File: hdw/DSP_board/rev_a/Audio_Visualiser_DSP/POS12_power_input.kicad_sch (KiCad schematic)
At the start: 21 parts, among them J201 +12V IN, U201 TPS26600RHFT

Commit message: cleared stale digikey part numbers
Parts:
- C201: Dielectric X5R -> X7R; Digi-Key PN 445-12201-1-ND -> (none)
- C202: Dielectric X5R -> X7R; Digi-Key PN 490-10697-1-ND -> (none)
- C203: Digi-Key PN 718-1102-1-ND -> (none)
- R201: Digi-Key PN RMCF0402FT51K1CT-ND -> (none)
- R202: Digi-Key PN RMCF0402FT1K15CT-ND -> (none)
- R203: Digi-Key PN RMCF0402FT5K11CT-ND -> (none)
- R204, R206, R211: Digi-Key PN RMCF0402FT10K0CT-ND -> (none)
- R205, R210: Digi-Key PN RMCF0402FT10R0CT-ND -> (none)
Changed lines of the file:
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@@
 			)
 		)
-		(property "Digi-Key PN" "RMCF0402FT5K11CT-ND"
+		(property "Digi-Key PN" ""
 			(at 85.09 100.33 0)
 			(hide yes)
@@
 			)
 		)
-		(property "Digi-Key PN" "RMCF0402FT10R0CT-ND"
+		(property "Digi-Key PN" ""
 			(at 157.48 48.26 0)
 			(hide yes)
@@
 			)
 		)
-		(property "Digi-Key PN" "490-10697-1-ND"
+		(property "Digi-Key PN" ""
 			(at 127.635 139.7 0)
 			(hide yes)
@@
 			)
 		)
-		(property "Dielectric" "X5R"
+		(property "Dielectric" "X7R"
 			(at 142.24 154.94 0)
 			(show_name no)
@@
 			)
 		)
-		(property "Digi-Key PN" "RMCF0402FT51K1CT-ND"
+		(property "Digi-Key PN" ""
 			(at 85.09 57.15 0)
 			(hide yes)
@@
 			)
 		)
-		(property "Digi-Key PN" "RMCF0402FT10K0CT-ND"
+		(property "Digi-Key PN" ""
 			(at 190.5 121.92 0)
 			(hide yes)
@@
 			)
 		)
-		(property "Digi-Key PN" "718-1102-1-ND"
+		(property "Digi-Key PN" ""
 			(at 212.09 62.23 0)
 			(hide yes)
@@
 			)
 		)
-		(property "Digi-Key PN" "RMCF0402FT10R0CT-ND"
+		(property "Digi-Key PN" ""
 			(at 170.18 48.26 0)
 			(hide yes)
@@
 			)
 		)
-		(property "Digi-Key PN" "RMCF0402FT10K0CT-ND"
+		(property "Digi-Key PN" ""
 			(at 170.18 121.92 0)
 			(hide yes)
@@
 			)
 		)
-		(property "Digi-Key PN" "RMCF0402FT1K15CT-ND"
+		(property "Digi-Key PN" ""
 			(at 85.09 78.74 0)
 			(hide yes)
@@
 			)
 		)
-		(property "Dielectric" "X5R"
+		(property "Dielectric" "X7R"
 			(at 109.22 113.03 0)
 			(show_name no)
@@
 			)
 		)
-		(property "Digi-Key PN" "445-12201-1-ND"
+		(property "Digi-Key PN" ""
 			(at 123.825 97.79 0)
 			(hide yes)
@@
 			)
 		)
-		(property "Digi-Key PN" "RMCF0402FT10K0CT-ND"
+		(property "Digi-Key PN" ""
 			(at 105.41 57.15 0)
 			(hide yes)

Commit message: assigned many digi-key part numbers
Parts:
- C201: Digi-Key PN (none) -> 490-4516-1-ND
- C202: Digi-Key PN (none) -> 1276-CL05B104KB5NNNCCT-ND
- C203: Digi-Key PN (none) -> 399-8410-1-ND; Voltage 16V -> 25V
- R201: Digi-Key PN (none) -> 311-51.1KLRCT-ND
- R202: Digi-Key PN (none) -> 311-1.15KLRCT-ND
- R203: Digi-Key PN (none) -> 311-5.11KLRCT-ND
- R204, R206, R208, R211: Digi-Key PN (none) -> 311-10.0KLRCT-ND
- R205, R210: Digi-Key PN (none) -> 311-10.0LRCT-ND
- R209: Digi-Key PN (none) -> 311-3.65KLRCT-ND
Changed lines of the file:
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@@
 			)
 		)
-		(property "Digi-Key PN" ""
+		(property "Digi-Key PN" "311-5.11KLRCT-ND"
 			(at 85.09 100.33 0)
 			(hide yes)
@@
 			)
 		)
-		(property "Digi-Key PN" ""
+		(property "Digi-Key PN" "311-10.0KLRCT-ND"
 			(at 163.83 99.06 0)
 			(hide yes)
@@
 			)
 		)
-		(property "Digi-Key PN" ""
+		(property "Digi-Key PN" "311-10.0LRCT-ND"
 			(at 157.48 48.26 0)
 			(hide yes)
@@
 			)
 		)
-		(property "Digi-Key PN" ""
+		(property "Digi-Key PN" "311-3.65KLRCT-ND"
 			(at 171.45 100.33 0)
 			(hide yes)
@@
 			)
 		)
-		(property "Digi-Key PN" ""
+		(property "Digi-Key PN" "1276-CL05B104KB5NNNCCT-ND"
 			(at 127.635 139.7 0)
 			(hide yes)
@@
 			)
 		)
-		(property "Digi-Key PN" ""
+		(property "Digi-Key PN" "311-51.1KLRCT-ND"
 			(at 85.09 57.15 0)
 			(hide yes)
@@
 			)
 		)
-		(property "Digi-Key PN" ""
+		(property "Digi-Key PN" "311-10.0KLRCT-ND"
 			(at 190.5 121.92 0)
 			(hide yes)
@@
 			)
 		)
-		(property "Digi-Key PN" ""
+		(property "Digi-Key PN" "399-8410-1-ND"
 			(at 212.09 62.23 0)
 			(hide yes)
@@
 			)
 		)
-		(property "Voltage" "16V"
+		(property "Voltage" "25V"
 			(at 208.28 62.23 0)
 			(show_name no)
@@
 			)
 		)
-		(property "Digi-Key PN" ""
+		(property "Digi-Key PN" "311-10.0LRCT-ND"
 			(at 170.18 48.26 0)
 			(hide yes)
@@
 			)
 		)
-		(property "Digi-Key PN" ""
+		(property "Digi-Key PN" "311-10.0KLRCT-ND"
 			(at 170.18 121.92 0)
 			(hide yes)
@@
 			)
 		)
-		(property "Digi-Key PN" ""
+		(property "Digi-Key PN" "311-1.15KLRCT-ND"
 			(at 85.09 78.74 0)
 			(hide yes)
@@
 			)
 		)
-		(property "Digi-Key PN" ""
+		(property "Digi-Key PN" "490-4516-1-ND"
 			(at 123.825 97.79 0)
 			(hide yes)
@@
 			)
 		)
-		(property "Digi-Key PN" ""
+		(property "Digi-Key PN" "311-10.0KLRCT-ND"
 			(at 105.41 57.15 0)
 			(hide yes)

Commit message: Defined legit KiCad BOM variants
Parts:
- R205, R210: now not fitted
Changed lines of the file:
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@@
 					(reference "R203")
 					(unit 1)
+					(variant
+						(name "Default")
+					)
+					(variant
+						(name "Development")
+					)
 				)
 			)
@@
 					(reference "U201")
 					(unit 1)
+					(variant
+						(name "Default")
+					)
+					(variant
+						(name "Development")
+					)
 				)
 			)
@@
 					(reference "R208")
 					(unit 1)
+					(variant
+						(name "Default")
+					)
+					(variant
+						(name "Development")
+					)
 				)
 			)
@@
 					(reference "N201")
 					(unit 1)
+					(variant
+						(name "Default")
+					)
+					(variant
+						(name "Development")
+					)
 				)
 			)
@@
 		(on_board yes)
 		(in_pos_files yes)
-		(dnp no)
+		(dnp yes)
 		(property "Reference" "R205"
 			(at 160.02 48.26 90)
@@
 					(reference "R205")
 					(unit 1)
+					(variant
+						(name "Default")
+					)
+					(variant
+						(name "Development")
+						(dnp no)
+					)
 				)
 			)
@@
 					(reference "R209")
 					(unit 1)
+					(variant
+						(name "Default")
+					)
+					(variant
+						(name "Development")
+					)
 				)
 			)
@@
 					(reference "J201")
 					(unit 1)
+					(variant
+						(name "Default")
+					)
+					(variant
+						(name "Development")
+					)
 				)
 			)
@@
 					(reference "C202")
 					(unit 1)
+					(variant
+						(name "Default")
+					)
+					(variant
+						(name "Development")
+					)
 				)
 			)
@@
 					(reference "R207")
 					(unit 1)
+					(variant
+						(name "Default")
+					)
+					(variant
+						(name "Development")
+					)
 				)
 			)
@@
 					(reference "R201")
 					(unit 1)
+					(variant
+						(name "Default")
+					)
+					(variant
+						(name "Development")
+					)
 				)
 			)
@@
 					(reference "TP201")
 					(unit 1)
+					(variant
+						(name "Default")
+					)
+					(variant
+						(name "Development")
+					)
 				)
 			)
@@
 					(reference "D201")
 					(unit 1)
+					(variant
+						(name "Default")
+					)
+					(variant
+						(name "Development")
+					)
 				)
 			)
@@
 					(reference "TP202")
 					(unit 1)
+					(variant
+						(name "Default")
+					)
+					(variant
+						(name "Development")
+					)
 				)
 			)
@@
 					(reference "R211")
 					(unit 1)
+					(variant
+						(name "Default")
+					)
+					(variant
+						(name "Development")
+					)
 				)
 			)
@@
 					(reference "TP203")
 					(unit 1)
+					(variant
+						(name "Default")
+					)
+					(variant
+						(name "Development")
+					)
 				)
 			)
@@
 					(reference "C203")
 					(unit 1)
+					(variant
+						(name "Default")
+					)
+					(variant
+						(name "Development")
+					)
 				)
 			)
@@
 		(on_board yes)
 		(in_pos_files yes)
-		(dnp no)
+		(dnp yes)
 		(property "Reference" "R210"
 			(at 172.72 48.26 90)
@@
 					(reference "R210")
 					(unit 1)
+					(variant
+						(name "Default")
+					)
+					(variant
+						(name "Development")
+						(dnp no)
+					)
 				)
 			)
@@
 					(reference "R206")
 					(unit 1)
+					(variant
+						(name "Default")
+					)
+					(variant
+						(name "Development")
+					)
 				)
 			)
@@
 					(reference "R202")
 					(unit 1)
+					(variant
+						(name "Default")
+					)
+					(variant
+						(name "Development")
+					)
 				)
 			)
@@
 					(reference "C201")
 					(unit 1)
+					(variant
+						(name "Default")
+					)
+					(variant
+						(name "Development")
+					)
 				)
 			)
@@
 					(reference "R204")
 					(unit 1)
+					(variant
+						(name "Default")
+					)
+					(variant
+						(name "Development")
+					)
 				)
 			)

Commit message: Added power draw tables
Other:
- note added: "1.2A is not enough, this device will most likely need to be changed"
- note added: "Explore shunt drop/dissipation at rated current"
- note removed: "TRY TO TALLY LOAD CURRENTS"

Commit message: update todo note for POS12
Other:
- note added: "Switch to TPS259474ARPW"
- note removed: "1.2A is not enough, this device will most likely need to be changed"
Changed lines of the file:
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@@
 		)
 	)
-	(text "1.2A is not enough, this device will most likely need to be changed"
+	(text "Switch to TPS259474ARPW"
 		(exclude_from_sim no)
 		(at 128.27 26.67 0)

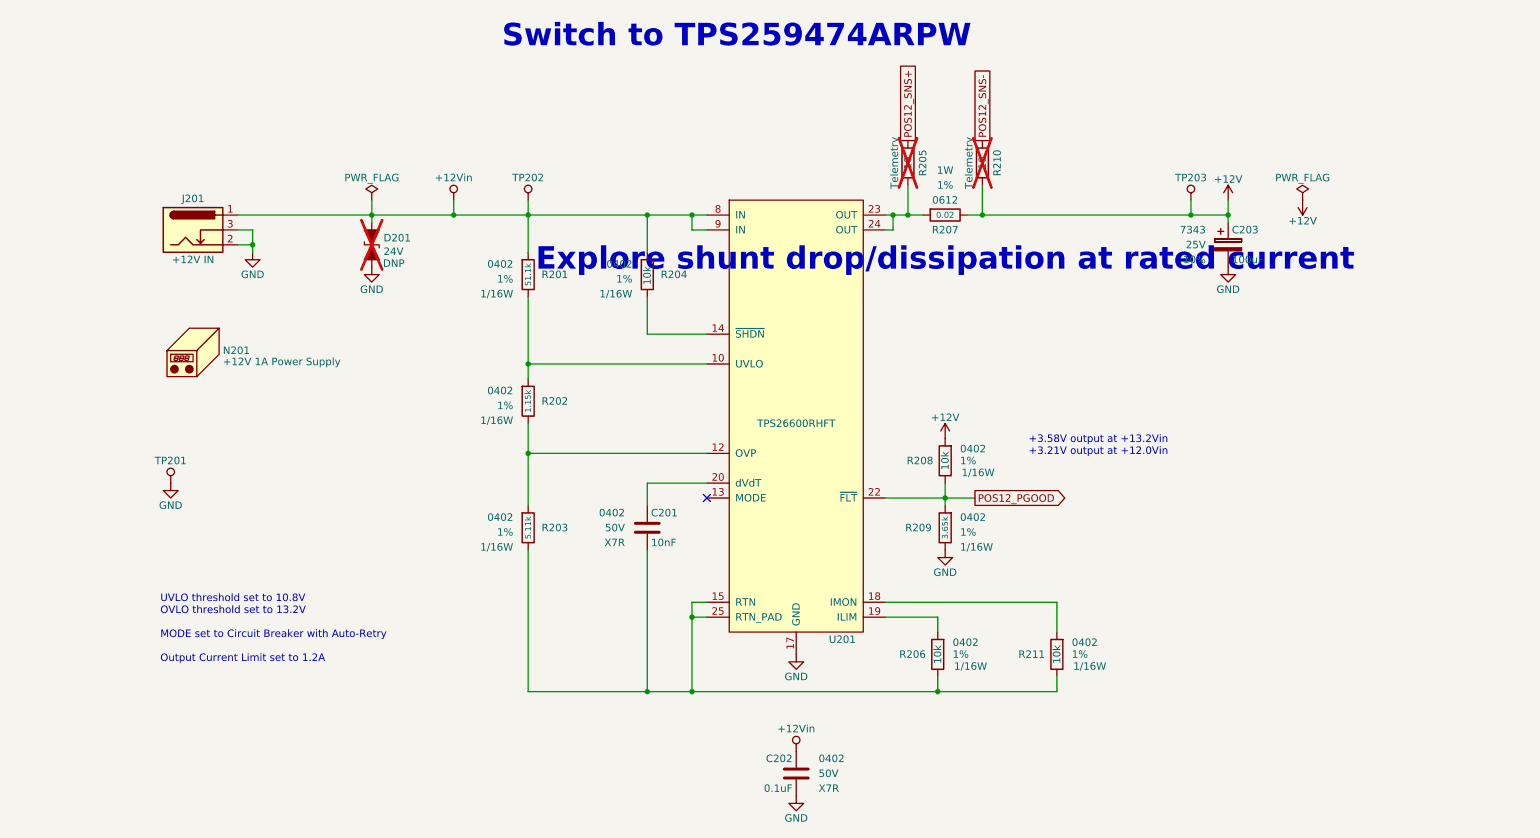
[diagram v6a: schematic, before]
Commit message: Updated input power sheet for higher currents
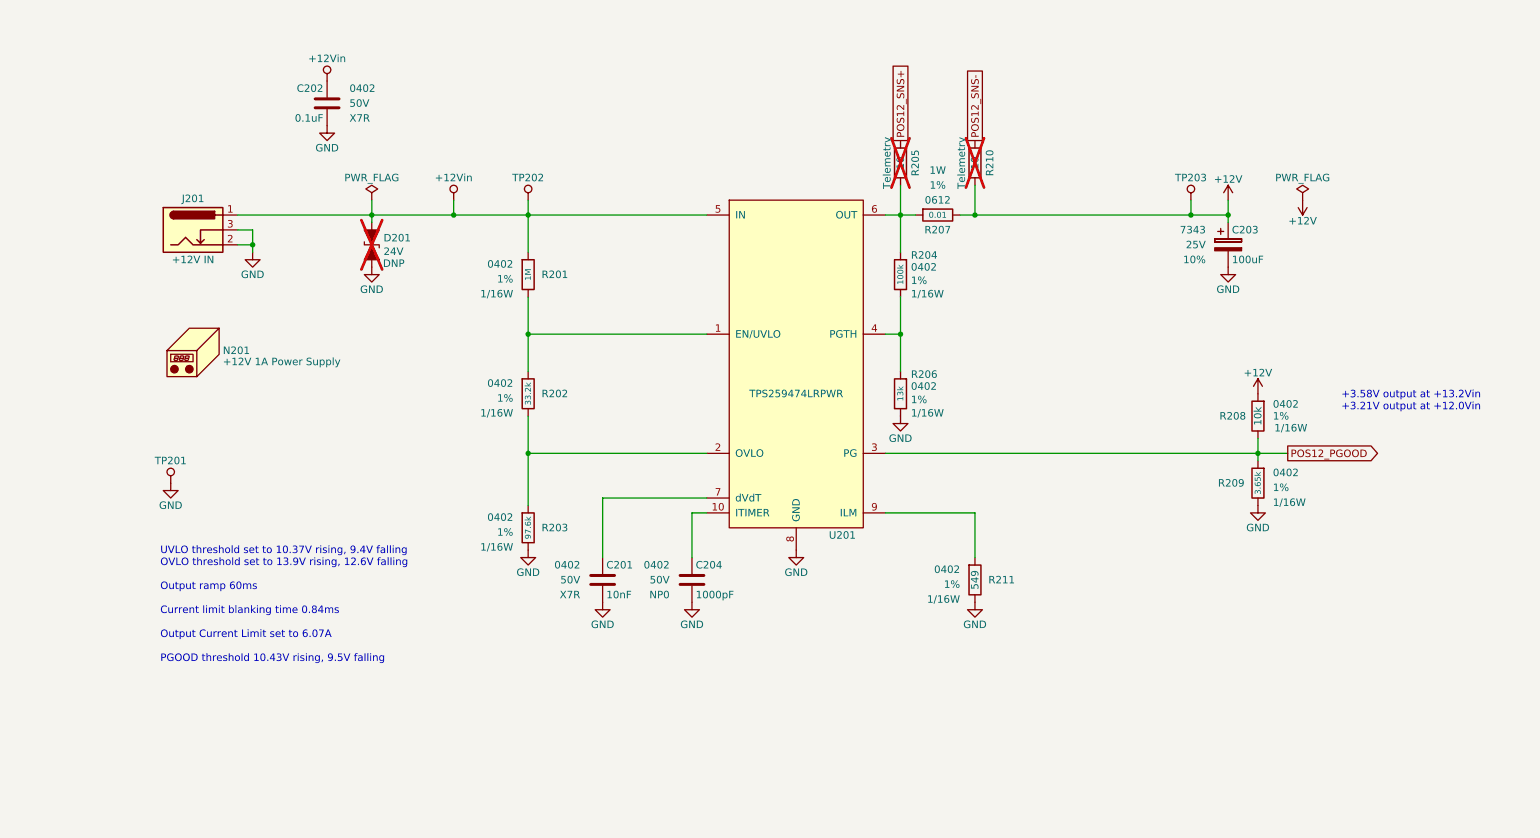
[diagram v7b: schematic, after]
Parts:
- removed U201: TPS26600RHFT, Housings_DFN_QFN:QFN-24-1EP_4x5mm_Pitch0.5mm, symbol Custom_Library:TPS26600RHFT
- added C204: 1000pF, Capacitors_SMD:C_0402, symbol Custom Library:C_Custom
- added U201: TPS259474LRPWR, symbol TPS259474:TPS259474LRPWR
- R201: value 51.1k -> 1M; Digi-Key PN 311-51.1KLRCT-ND -> (none)
- R202: value 1.15k -> 33.2k; Digi-Key PN 311-1.15KLRCT-ND -> (none)
- R203: value 5.11k -> 97.6k; Digi-Key PN 311-5.11KLRCT-ND -> (none)
- R204: value 10k -> 100k; Digi-Key PN 311-10.0KLRCT-ND -> 311-100KLRCT-ND
- R206: value 10k -> 13k; Digi-Key PN 311-10.0KLRCT-ND -> (none)
- R207: value 0.02 -> 0.01; Digi-Key PN P16010CT-ND -> 10-ERJ-B2CFR01VCT-ND
- R211: value 10k -> 549; Digi-Key PN 311-10.0KLRCT-ND -> (none)
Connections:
- net +12Vin: now also U201.5 (IN); no longer R204.1
- net GND: now also C201.2, R203.2, R206.2, R211.2, C204.2, U201.8 (GND)
- net POS12_PGOOD: now also U201.3 (PG)
- net at R202.2, R203.1: now also U201.2 (OVLO)
- net at R201.2, R202.1: now also U201.1 (EN/UVLO)
- net at R204.2: now also R206.1, U201.4 (PGTH)
- net at R211.1: now also U201.9 (ILM)
- net at C201.1: now also U201.7 (dVdT)
- net at R205.2, R207.1: now also R204.1, U201.6 (OUT)
- new net: C204.1, U201.10 (ITIMER)
- no-connect marks 1 -> 0
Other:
- note added: "UVLO threshold set to 10.37V rising, 9.4V falling OVLO threshold set to 13.9V rising, 12.6V falling Output ramp 60ms Current limit blanking time 0.84ms Output Current Limit set to 6.07A PGOOD threshold 10.43V rising, 9.5V falling"
- note removed: "Explore shunt drop/dissipation at rated current"
- note removed: "Switch to TPS259474ARPW"
- note removed: "UVLO threshold set to 10.8V OVLO threshold set to 13.2V MODE set to Circuit Breaker with Auto-Retry Output Current Limit set to 1.2A"
- moved on the sheet: C202, R202, R205, R207, R208, R209, R210

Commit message: add footprint for efuse, change PSU part number to 5A brick
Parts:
- N201: value +12V 1A Power Supply -> +12V 5A Power Supply; Digi-Key PN 993-1335-ND -> 5942-YS50-1205000-D1J-C14-ND
- U201: footprint (none) -> TPS259474:Texas_RPW0010A_VQFN-HR-10_2x2mm_P0.45mm
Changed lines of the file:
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@@
 			)
 		)
-		(property "Value" "+12V 1A Power Supply"
+		(property "Value" "+12V 5A Power Supply"
 			(at 40.64 82.169 0)
 			(show_name no)
@@
 			)
 		)
-		(property "Digi-Key PN" "993-1335-ND"
+		(property "Digi-Key PN" "5942-YS50-1205000-D1J-C14-ND"
 			(at 36.83 80.264 0)
 			(hide yes)
@@
 			)
 		)
-		(property "Footprint" ""
+		(property "Footprint" "TPS259474:Texas_RPW0010A_VQFN-HR-10_2x2mm_P0.45mm"
 			(at 138.43 100.076 0)
 			(hide yes)
